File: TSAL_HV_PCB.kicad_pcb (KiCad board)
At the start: 2 copper layers, 100 x 40 mm, 40 parts, among them J3 Conn_01x03_Socket, J4 Conn_01x03_Socket, K1 SPU01M-12, U1 LM393, U2 4N35, U3 TPS7B88-Q1

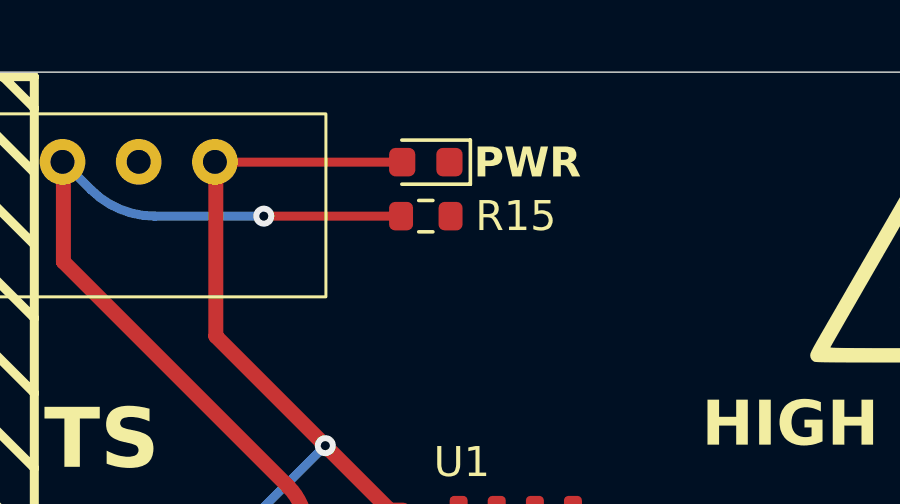
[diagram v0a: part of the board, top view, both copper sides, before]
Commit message: Fixed unconnected trace
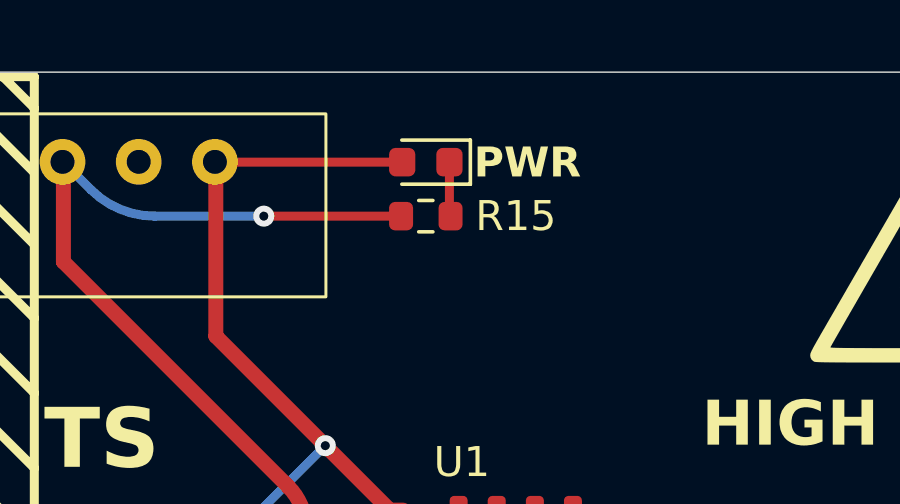
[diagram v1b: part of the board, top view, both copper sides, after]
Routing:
- net Net-(D8-K): track 0.00 -> 1.82 mm
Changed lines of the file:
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@@
+	)
+	(segment
+		(start 189.187501 58)
+		(end 189.187501 59.762501)
+		(width 0.3)
+		(layer "F.Cu")
+		(net 26)
+	)
+	(segment
+		(start 189.187501 59.762501)
+		(end 189.225 59.8)
+		(width 0.3)
+		(layer "F.Cu")
+		(net 26)
 	)
 	(segment

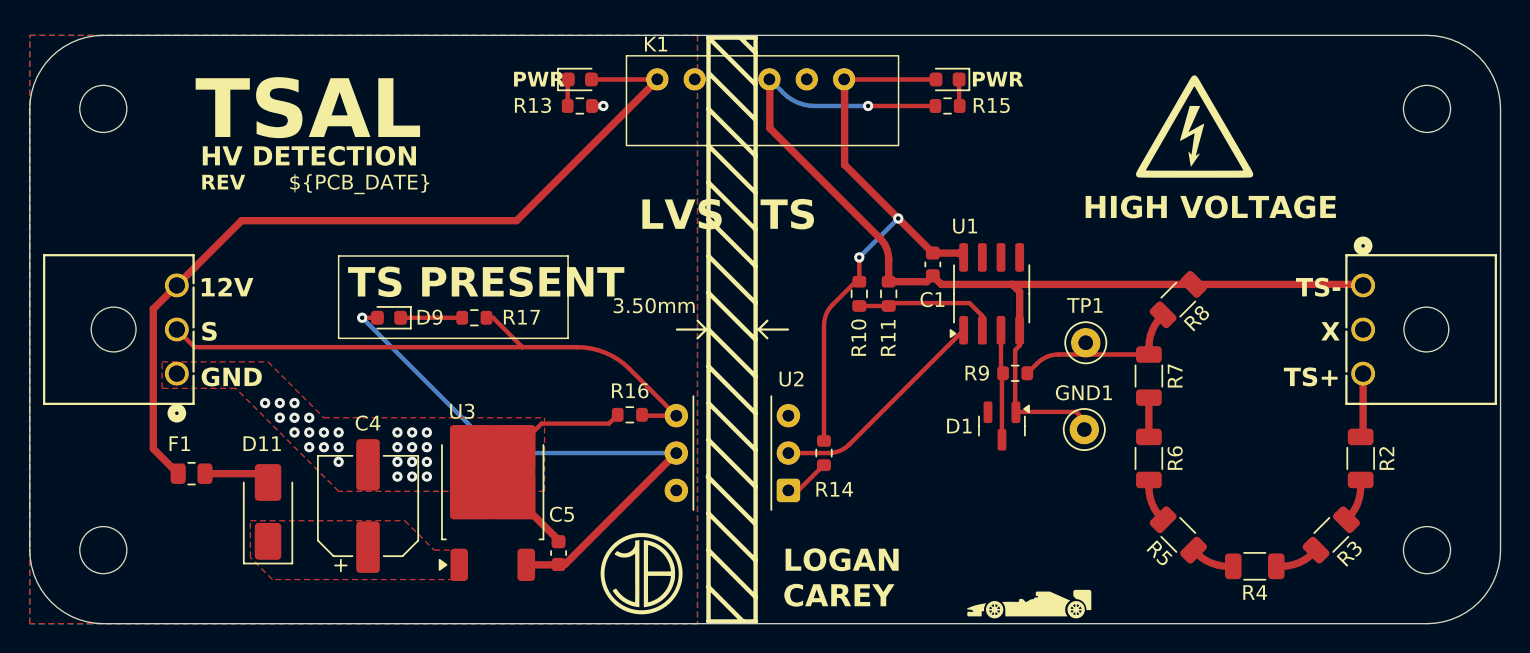
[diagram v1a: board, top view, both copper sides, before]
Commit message: Changed LED Indicator, updated footprints
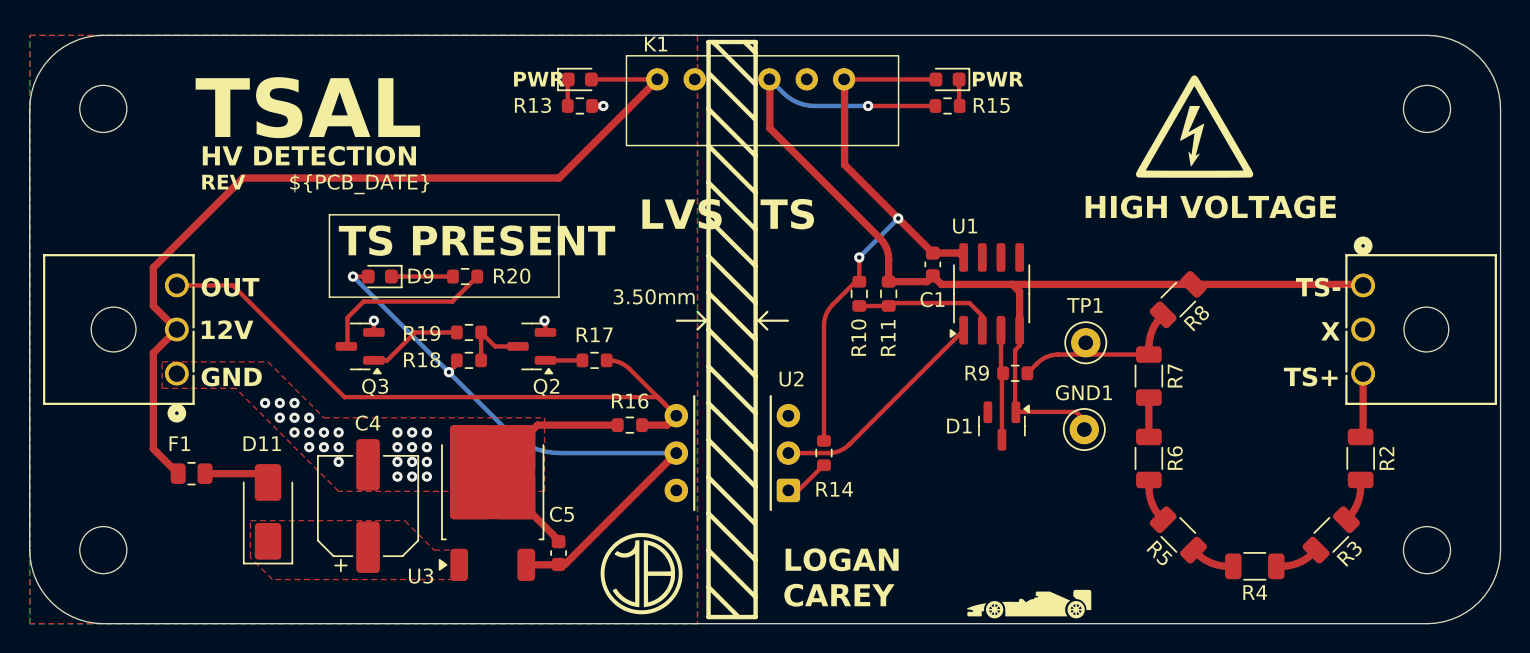
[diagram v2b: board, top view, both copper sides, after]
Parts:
- added Q2: 2N7002, Package_TO_SOT_SMD:SOT-23, F.Cu at (160.1, 76.2)
- added Q3: 2N7002, Package_TO_SOT_SMD:SOT-23, F.Cu at (148.5, 76.2)
- added R18: 10k, Resistor_SMD:R_0603_1608Metric, F.Cu at (155.9, 77.1)
- added R19: 200, Resistor_SMD:R_0603_1608Metric, F.Cu at (155.9, 75.2)
- added R20: 330, Resistor_SMD:R_0603_1608Metric, F.Cu at (155.6, 71.4)
- D9: value LED_Small -> LED
- J3, J4: footprint MyLibrary:MolexMicrofitPlus1x3 -> yfs:MolexMicrofitPlus1x3
- K1: footprint MyLibrary:SPU01M-12 -> yfs:SPU01M-12
- R14: value 1k -> 2.4k
- R17: value 10k -> 200
- moved R17 8.67 mm to (164.4, 77.1), turned to 180 degrees
- moved D9 2.87 mm to (149.8, 71.4)
- moved R16 0.70 mm to (166.8, 81.5)
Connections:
- J3 pad 2: 60V_Detect -> +12V
- J3 pad 3: +12V -> 60V_Detect
- R17 pad 1: Net-(D9-K) -> 60V_Detect
- R17 pad 2: 60V_Detect -> Net-(Q2-G)
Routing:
- net Net-(Q3-D): track 0.00 -> 12.0 mm
- net Net-(Q3-G): track 0.00 -> 6.42 mm
- net Net-(Q2-D): track 0.00 -> 4.79 mm
- net 60V_Detect: track 41.8 -> 46.4 mm
- net +5V: track 39.3 -> 42.1 mm, vias 1 -> 2
- net Net-(Q2-G): track 0.00 -> 2.51 mm
- net +12V: track 57.2 -> 59.6 mm
- net GND: track 16.3 -> 17.8 mm, vias 27 -> 29
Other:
- board text added: "OUT"
- board text removed: "S"

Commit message: Changed DC-DC Converter
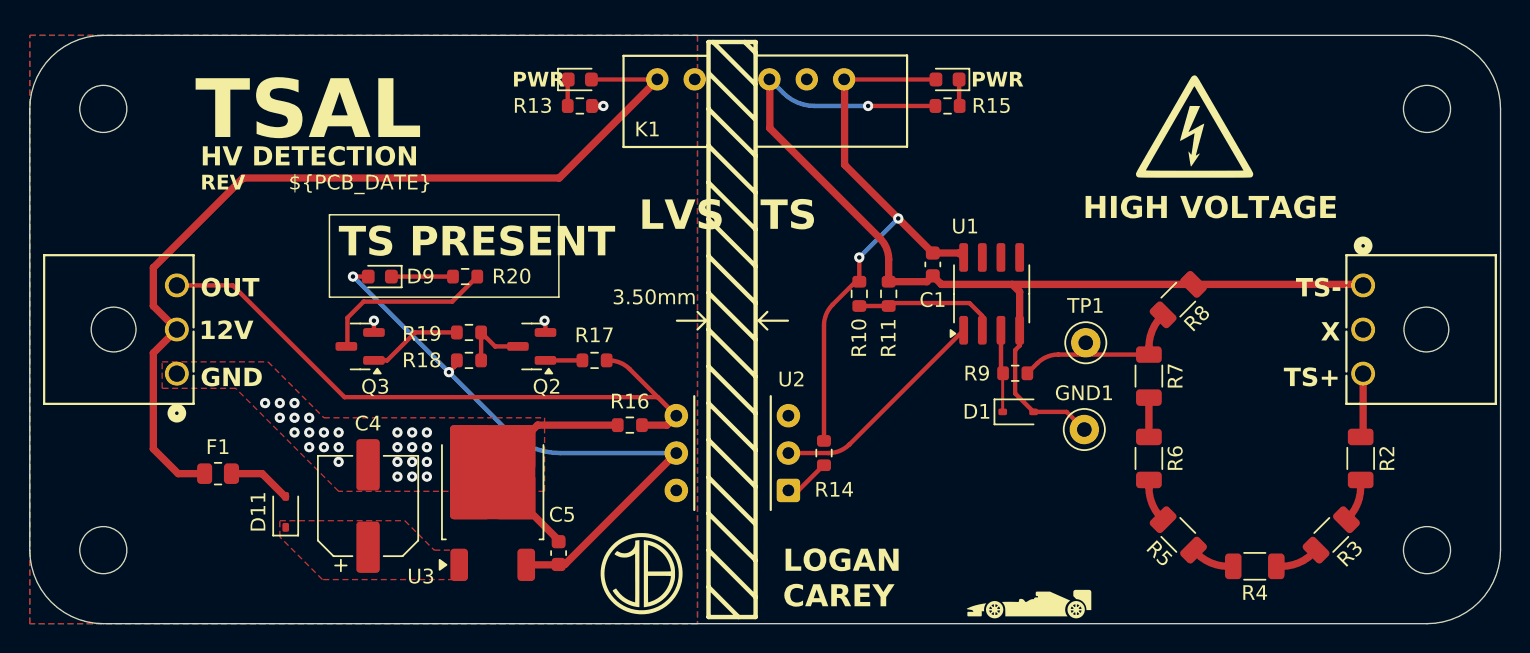
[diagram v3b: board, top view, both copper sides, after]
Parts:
- D1: value BZX84Cxx -> BZX384xxxx; footprint Package_TO_SOT_SMD:SOT-23 -> Diode_SMD:D_SOD-323
- D11: value SS34 -> NSR0530HT1G; footprint Diode_SMD:D_SMA -> Diode_SMD:D_SOD-323
- K1: value SPU01M-12 -> SPU01M-5; footprint yfs:SPU01M-12 -> yfs:SPU01M-5
- R14: value 2.4k -> 1.8k
- R15: value 10k -> 1k
- moved F1 1.80 mm to (138.8, 84.8)
- moved D1 1.46 mm to (193.2, 80.6), turned to 0 degrees
- moved D11 1.20 mm to (143.4, 87.4)
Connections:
- net +12VA renamed +5VA
- D1 pad 1: HV- -> Net-(D1-K)
- D1 pad 2: unconnected-(D1-NC-Pad2) -> HV-
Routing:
- net Net-(D1-K): track 7.57 -> 5.76 mm
- net +12V: track 59.6 -> 61.4 mm

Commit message: Polyfuse for DC-DC supply
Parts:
- added F2: 500mA, Resistor_SMD:R_0805_2012Metric, F.Cu at (163.2, 63.0)
- F1: value Polyfuse -> 100mA
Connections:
- K1 pad 1: +12V -> Net-(K1-+Vin)
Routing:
- net +12V: track 61.4 -> 25.9 mm
- net Net-(K1-+Vin): track 0.00 -> 6.90 mm
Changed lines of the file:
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@@
 	(net 29 "Net-(Q3-G)")
 	(net 30 "+5VA")
+	(net 31 "Net-(K1-+Vin)")
 	(footprint "yfs:SPU01M-5"
 		(layer "F.Cu")
@@
 			(layers "*.Cu" "*.Mask")
 			(remove_unused_layers no)
-			(net 6 "+12V")
+			(net 31 "Net-(K1-+Vin)")
 			(pinfunction "+Vin")
 			(pintype "input")
@@
 		(embedded_fonts no)
 	)
+	(footprint "Resistor_SMD:R_0805_2012Metric"
+		(layer "F.Cu")
+		(at 163.2 63 180)
+		(descr "Resistor SMD 0805 (2012 Metric), square (rectangular) end terminal, IPC_7351 nominal, (Body size source: IPC-SM-782 page 72, https://www.pcb-3d.com/wordpress/wp-content/uploads/ipc-sm-782a_amendment_1_and_2.pdf), generated with kicad-footprint-generator")
+		(tags "resistor")
+		(property "Reference" "F2"
+			(at 2.9125 0 0)
+			(layer "F.SilkS")
+			(effects
+				(font
+					(size 1 1)
+					(thickness 0.15)
+				)
+			)
+		)
+		(property "Value" "500mA"
+			(at 0 1.65 0)
+			(layer "F.Fab")
+			(effects
+				(font
+					(size 1 1)
+					(thickness 0.15)
+				)
+			)
+		)
+		(property "Datasheet" ""
+			(at 0 0 180)
+			(unlocked yes)
+			(layer "F.Fab")
+			(hide yes)
+			(effects
+				(font
+					(size 1.27 1.27)
+					(thickness 0.15)
+				)
+			)
+		)
+		(property "Description" "Resettable fuse, polymeric positive temperature coefficient"
+			(at 0 0 180)
+			(unlocked yes)
+			(layer "F.Fab")
+			(hide yes)
+			(effects
+				(font
+					(size 1.27 1.27)
+					(thickness 0.15)
+				)
+			)
+		)
+		(property ki_fp_filters "*polyfuse* *PTC*")
+		(sheetname "/")
+		(sheetfile "TSAL_HV_PCB.kicad_sch")
+		(attr smd)
+		(fp_line
+			(start -0.227064 0.735)
+			(end 0.227064 0.735)
+			(stroke
+				(width 0.12)
+				(type solid)
+			)
+			(layer "F.SilkS")
+		)
+		(fp_line
+			(start -0.227064 -0.735)
+			(end 0.227064 -0.735)
+			(stroke
+				(width 0.12)
+				(type solid)
+			)
+			(layer "F.SilkS")
+		)
+		(fp_line
+			(start 1.68 0.95)
+			(end -1.68 0.95)
+			(stroke
+				(width 0.05)
+				(type solid)
+			)
+			(layer "F.CrtYd")
+		)
+		(fp_line
+			(start 1.68 -0.95)
+			(end 1.68 0.95)
+			(stroke
+				(width 0.05)
+				(type solid)
+			)
+			(layer "F.CrtYd")
+		)
+		(fp_line
+			(start -1.68 0.95)
+			(end -1.68 -0.95)
+			(stroke
+				(width 0.05)
+				(type solid)
+			)
+			(layer "F.CrtYd")
+		)
+		(fp_line
+			(start -1.68 -0.95)
+			(end 1.68 -0.95)
+			(stroke
+				(width 0.05)
+				(type solid)
+			)
+			(layer "F.CrtYd")
+		)
+		(fp_line
+			(start 1 0.625)
+			(end -1 0.625)
+			(stroke
+				(width 0.1)
+				(type solid)
+			)
+			(layer "F.Fab")
+		)
+		(fp_line
+			(start 1 -0.625)
+			(end 1 0.625)
+			(stroke
+				(width 0.1)
+				(type solid)
+			)
+			(layer "F.Fab")
+		)
+		(fp_line
+			(start -1 0.625)
+			(end -1 -0.625)
+			(stroke
+				(width 0.1)
+				(type solid)
+			)
+			(layer "F.Fab")
+		)
+		(fp_line
+			(start -1 -0.625)
+			(end 1 -0.625)
+			(stroke
+				(width 0.1)
+				(type solid)
+			)
+			(layer "F.Fab")
+		)
+		(fp_text user "${REFERENCE}"
+			(at 0 0 0)
+			(layer "F.Fab")
+			(effects
+				(font
+					(size 0.5 0.5)
+					(thickness 0.08)
+				)
+			)
+		)
+		(pad "1" smd roundrect
+			(at -0.9125 0 180)
+			(size 1.025 1.4)
+			(layers "F.Cu" "F.Mask" "F.Paste")
+			(roundrect_rratio 0.243902)
+			(net 31 "Net-(K1-+Vin)")
+			(pintype "passive")
+		)
+		(pad "2" smd roundrect
+			(at 0.9125 0 180)
+			(size 1.025 1.4)
+			(layers "F.Cu" "F.Mask" "F.Paste")
+			(roundrect_rratio 0.243902)
+			(net 6 "+12V")
+			(pintype "passive")
+		)
+		(embedded_fonts no)
+		(model "${KICAD9_3DMODEL_DIR}/Resistor_SMD.3dshapes/R_0805_2012Metric.wrl"
+			(offset
+				(xyz 0 0 0)
+			)
+			(scale
+				(xyz 1 1 1)
+			)
+			(rotate
+				(xyz 0 0 0)
+			)
+		)
+	)
 	(footprint "Resistor_SMD:R_1206_3216Metric"
 		(layer "F.Cu")
@@
 			)
 		)
-		(property "Value" "Polyfuse"
+		(property "Value" "100mA"
 			(at 0 1.65 0)
 			(layer "F.Fab")
@@
 	)
 	(segment
-		(start 168.7 58)
-		(end 162 64.7)
-		(width 0.5)
-		(layer "F.Cu")
-		(net 6)
-	)
-	(segment
 		(start 134.4 83.1125)
 		(end 136.0875 84.8)
@@
 	)
 	(segment
-		(start 164.1875 58)
-		(end 168.7 58)
-		(width 0.3)
-		(layer "F.Cu")
-		(net 6)
-	)
-	(segment
 		(start 140.5 64.7)
 		(end 134.4 70.8)
@@
 	)
 	(segment
-		(start 162 64.7)
-		(end 140.5 64.7)
-		(width 0.5)
-		(layer "F.Cu")
-		(net 6)
-	)
-	(segment
 		(start 162.575 59.8)
 		(end 162.575 58.0375)
@@
 		(net 30)
 	)
+	(segment
+		(start 164.1125 62.5475)
+		(end 168.67 57.99)
+		(width 0.5)
+		(layer "F.Cu")
+		(net 31)
+	)
+	(segment
+		(start 164.1125 63)
+		(end 164.1125 62.5475)
+		(width 0.5)
+		(layer "F.Cu")
+		(net 31)
+	)
 	(zone
